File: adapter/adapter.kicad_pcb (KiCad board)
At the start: 4 copper layers, 28 x 28 mm, 9 parts, among them U1 TPS61041DBV

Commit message: add URL
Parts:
- moved REF** 1.77 mm to (112.2, 72.8)
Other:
- board text added: "https://calculinux.org/"
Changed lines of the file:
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@@
 	(footprint "Symbol:OSHW-Logo2_9.8x8mm_SilkScreen"
 		(layer "F.Cu")
-		(at 112 74.5)
+		(at 112.25 72.75)
 		(descr "Open Source Hardware Symbol")
 		(tags "Logo Symbol OSHW")
@@
 		(layer "Edge.Cuts")
 	)
+	(gr_text "https://calculinux.org/"
+		(at 103.5 78 0)
+		(layer "F.SilkS")
+		(effects
+			(font
+				(size 1 1)
+				(thickness 0.1)
+			)
+			(justify left bottom)
+		)
+	)
 	(segment

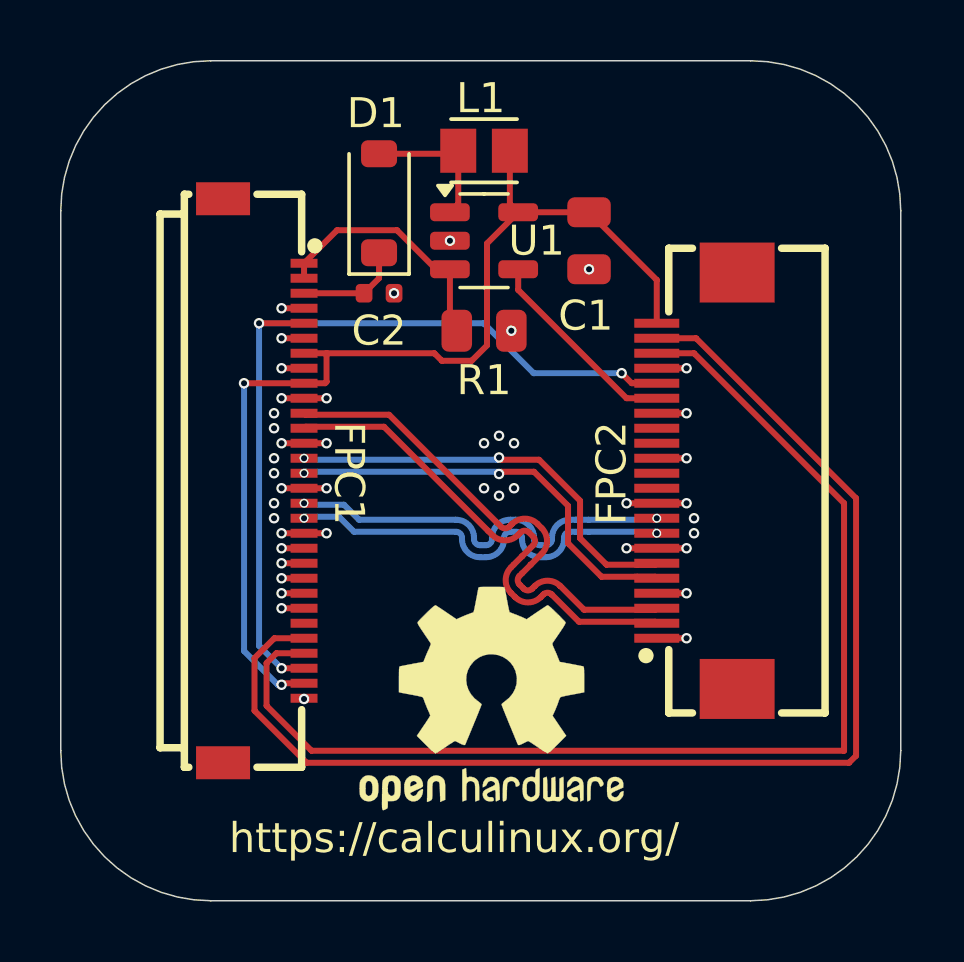
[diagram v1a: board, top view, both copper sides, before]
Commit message: fix a few messed up traces, pass DRU
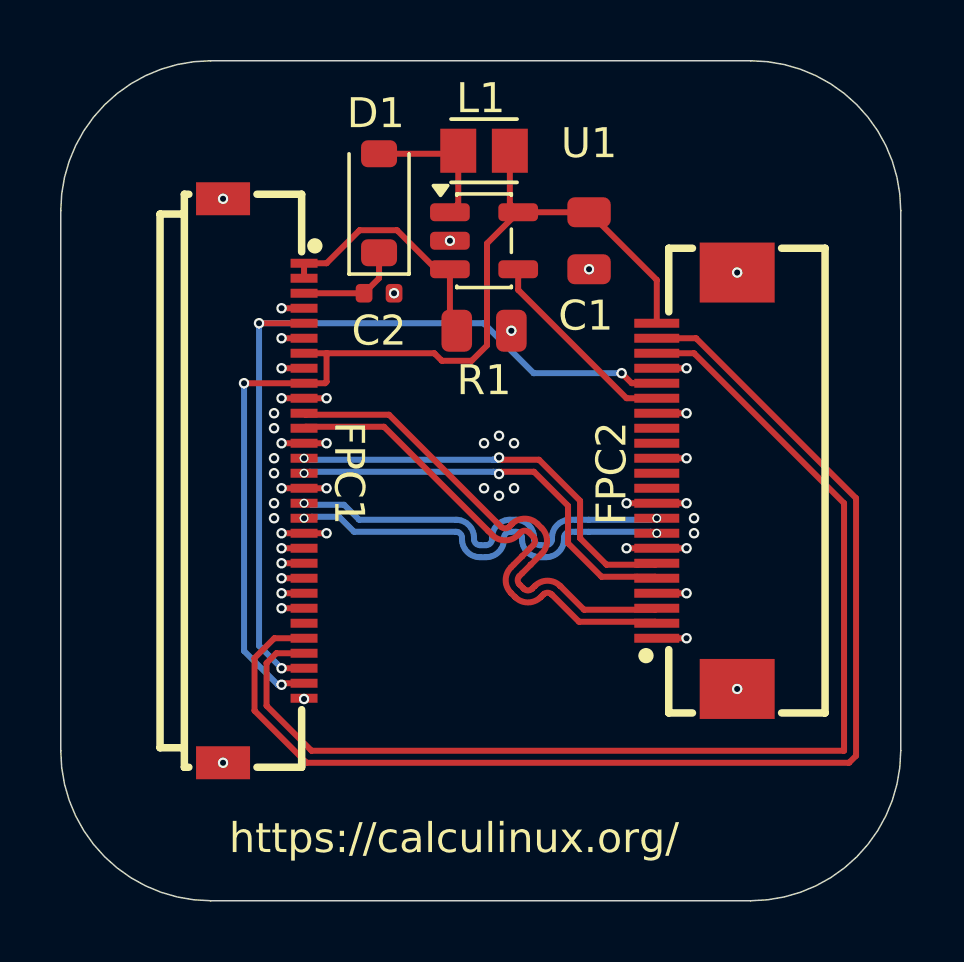
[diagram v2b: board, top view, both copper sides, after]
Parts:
- removed REF**: OSHW-Logo2_9.8x8mm_SilkScreen, Symbol:OSHW-Logo2_9.8x8mm_SilkScreen
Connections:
- FPC1 pad 31: (no net) -> GND
- FPC1 pad 32: (no net) -> GND
- FPC2 pad 23: unconnected-(FPC2-Pad23) -> GND
- FPC2 pad 24: unconnected-(FPC2-Pad24) -> GND
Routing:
- net GND: vias 44 -> 48
